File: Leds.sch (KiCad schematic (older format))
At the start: 46 parts, among them U4 MAX7219

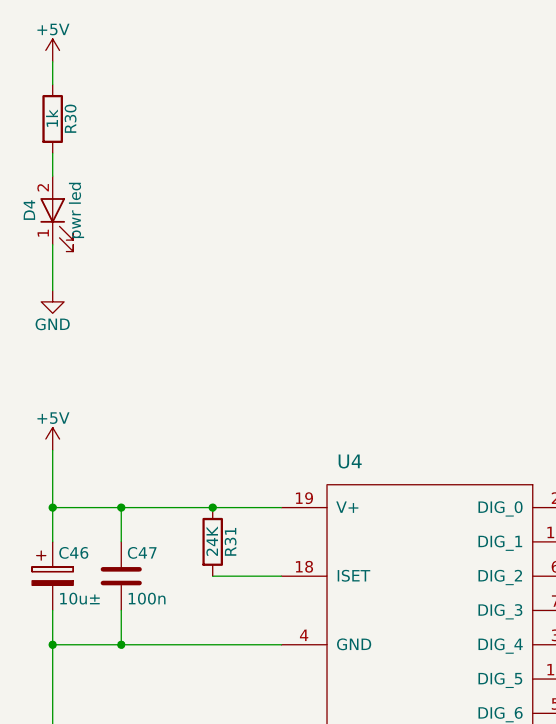
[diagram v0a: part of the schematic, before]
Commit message: Board should be ok. Bargraph leds yet to do.
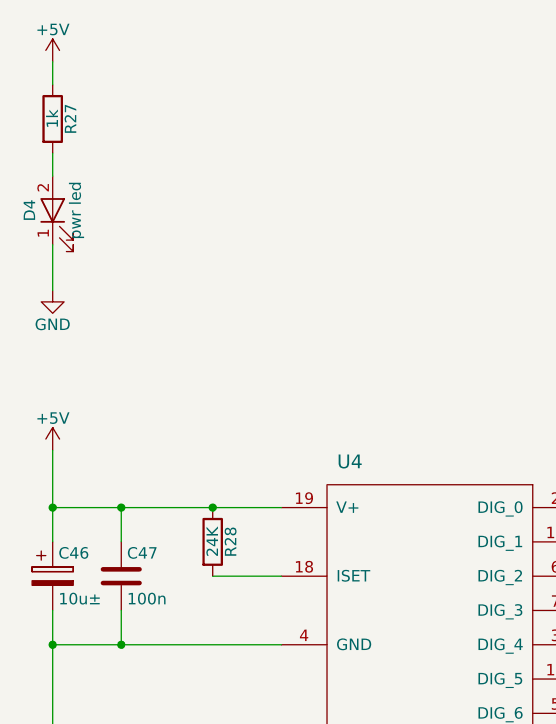
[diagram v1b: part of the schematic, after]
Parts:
- renumbered R30 to R27, R31 to R28
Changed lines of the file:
@@
 $EndComp
 $Comp
-L R R31
+L R R28
 U 1 1 59A6F7DE
 P 2450 3100
-F 0 "R31" V 2530 3100 50  0000 C CNN
+F 0 "R28" V 2530 3100 50  0000 C CNN
 F 1 "24K" V 2450 3100 50  0000 C CNN
 F 2 "Resistors_SMD:R_0603" V 2380 3100 50  0001 C CNN
@@
 	1750 2000 1750 1800
 $Comp
-L R R30
+L R R27
 U 1 1 59C8EB45
 P 1750 1250
-F 0 "R30" V 1830 1250 50  0000 C CNN
+F 0 "R27" V 1830 1250 50  0000 C CNN
 F 1 "1k" V 1750 1250 50  0000 C CNN
 F 2 "Resistors_SMD:R_0603" V 1680 1250 50  0001 C CNN

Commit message: Seems to be good for fabrication launch. Probably minor things to fix.
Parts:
- removed D43: ST_01, LEDs:LED_0603, symbol LED
- removed D44: ST_00, LEDs:LED_0603, symbol LED
- added J7: Display - secondary, Connectors_perso:Hirose_FH12-16S-1_SH, symbol Conn_01x16
- added J8: Display - main, Connectors_perso:Hirose_FH12-16S-1_SH, symbol Conn_01x16
- D10: value VU_10 -> VU_05
- D11: value VU_09 -> VU_06
- D12: value VU_08 -> VU_07
- D13: value VU_07 -> VU_08
- D14: value VU_06 -> VU_09
- D15: value VU_05 -> VU_10
- D16: value VU_04 -> VU_11
- D17: value VU_03 -> VU_12
- D18: value VU_02 -> VU_13
- D19: value VU_01 -> VU_14
- D20: value VU_00 -> VU_15
- D21: value VU_31 -> VU_16
- D22: value VU_30 -> VU_17
- D23: value VU_29 -> VU_18
- D24: value VU_28 -> VU_19
- D25: value VU_27 -> VU_20
- D26: value VU_26 -> VU_21
- D27: value VU_25 -> VU_22
- D28: value VU_24 -> VU_23
- D29: value VU_23 -> VU_24
- D30: value VU_22 -> VU_25
- D31: value VU_21 -> VU_26
- D32: value VU_20 -> VU_27
- D33: value VU_19 -> VU_28
- D34: value VU_18 -> VU_29
- D35: value VU_17 -> VU_30
- D36: value VU_16 -> VU_31
- D37: value ST_07 -> ST_00
- D38: value ST_06 -> ST_01
- D39: value ST_05 -> ST_02
- D40: value ST_04 -> ST_03
- D41: value ST_03 -> ST_04
- D42: value ST_02 -> ST_05
- D5: value VU_15 -> VU_00
- D6: value VU_14 -> VU_01
- D7: value VU_13 -> VU_02
- D8: value VU_12 -> VU_03
- D9: value VU_11 -> VU_04
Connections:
- net +5V: now also J7.15 (Pin_15), J8.2 (Pin_2)
- net DIG_0: now also D10.1 (K), D11.1 (K), D12.1 (K), D5.1 (K), D6.1 (K), D7.1 (K), D8.1 (K), D9.1 (K), J7.9 (Pin_9), J8.8 (Pin_8); no longer D13.1 (K), D14.1 (K), D15.1 (K), D16.1 (K), D17.1 (K), D18.1 (K), D19.1 (K), D20.1 (K)
- net DIG_1: now also D13.1 (K), D14.1 (K), D15.1 (K), D16.1 (K), D17.1 (K), D18.1 (K), D19.1 (K), D20.1 (K), J7.10 (Pin_10), J8.7 (Pin_7); no longer D10.1 (K), D11.1 (K), D12.1 (K), D5.1 (K), D6.1 (K), D7.1 (K), D8.1 (K), D9.1 (K)
- net DIG_2: now also D21.1 (K), D22.1 (K), D23.1 (K), D24.1 (K), D25.1 (K), D26.1 (K), D27.1 (K), D28.1 (K), J7.11 (Pin_11), J8.6 (Pin_6); no longer D29.1 (K), D30.1 (K), D31.1 (K), D32.1 (K), D33.1 (K), D34.1 (K), D35.1 (K), D36.1 (K)
- net DIG_3: now also D29.1 (K), D30.1 (K), D31.1 (K), D32.1 (K), D33.1 (K), D34.1 (K), D35.1 (K), D36.1 (K), J7.12 (Pin_12), J8.5 (Pin_5); no longer D21.1 (K), D22.1 (K), D23.1 (K), D24.1 (K), D25.1 (K), D26.1 (K), D27.1 (K), D28.1 (K)
- net DIG_4: now also J7.13 (Pin_13), J8.4 (Pin_4)
- net GND: now also J7.16 (Pin_16), J8.1 (Pin_1)
- net SEG_A: now also D11.2 (A), D19.2 (A), D27.2 (A), D35.2 (A), J7.7 (Pin_7), J8.10 (Pin_10); no longer D14.2 (A), D22.2 (A), D30.2 (A), D38.2 (A), D6.2 (A)
- net SEG_B: now also D10.2 (A), D18.2 (A), D26.2 (A), D34.2 (A), D42.2 (A), J7.6 (Pin_6), J8.11 (Pin_11); no longer D15.2 (A), D23.2 (A), D31.2 (A), D39.2 (A), D7.2 (A)
- net SEG_C: now also D17.2 (A), D25.2 (A), D33.2 (A), D41.2 (A), D9.2 (A), J7.5 (Pin_5), J8.12 (Pin_12); no longer D16.2 (A), D24.2 (A), D32.2 (A), D40.2 (A), D8.2 (A)
- net SEG_D: now also D16.2 (A), D24.2 (A), D32.2 (A), D40.2 (A), D8.2 (A), J7.4 (Pin_4), J8.13 (Pin_13); no longer D17.2 (A), D25.2 (A), D33.2 (A), D41.2 (A), D9.2 (A)
- net SEG_DP: now also D12.2 (A), D20.2 (A), D28.2 (A), D36.2 (A), J7.8 (Pin_8), J8.9 (Pin_9); no longer D13.2 (A), D21.2 (A), D29.2 (A), D37.2 (A), D5.2 (A)
- net SEG_E: now also D15.2 (A), D23.2 (A), D31.2 (A), D39.2 (A), D7.2 (A), J7.3 (Pin_3), J8.14 (Pin_14); no longer D10.2 (A), D18.2 (A), D26.2 (A), D34.2 (A), D42.2 (A)
- net SEG_F: now also D14.2 (A), D22.2 (A), D30.2 (A), D38.2 (A), D6.2 (A), J7.2 (Pin_2), J8.15 (Pin_15); no longer D11.2 (A), D19.2 (A), D27.2 (A), D35.2 (A)
- net SEG_G: now also D13.2 (A), D21.2 (A), D29.2 (A), D37.2 (A), D5.2 (A), J7.1 (Pin_1), J8.16 (Pin_16); no longer D12.2 (A), D20.2 (A), D28.2 (A), D36.2 (A)
- no-connect marks 4 -> 6
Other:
- moved on the sheet: C46, C47, D4, R27, R28, U4

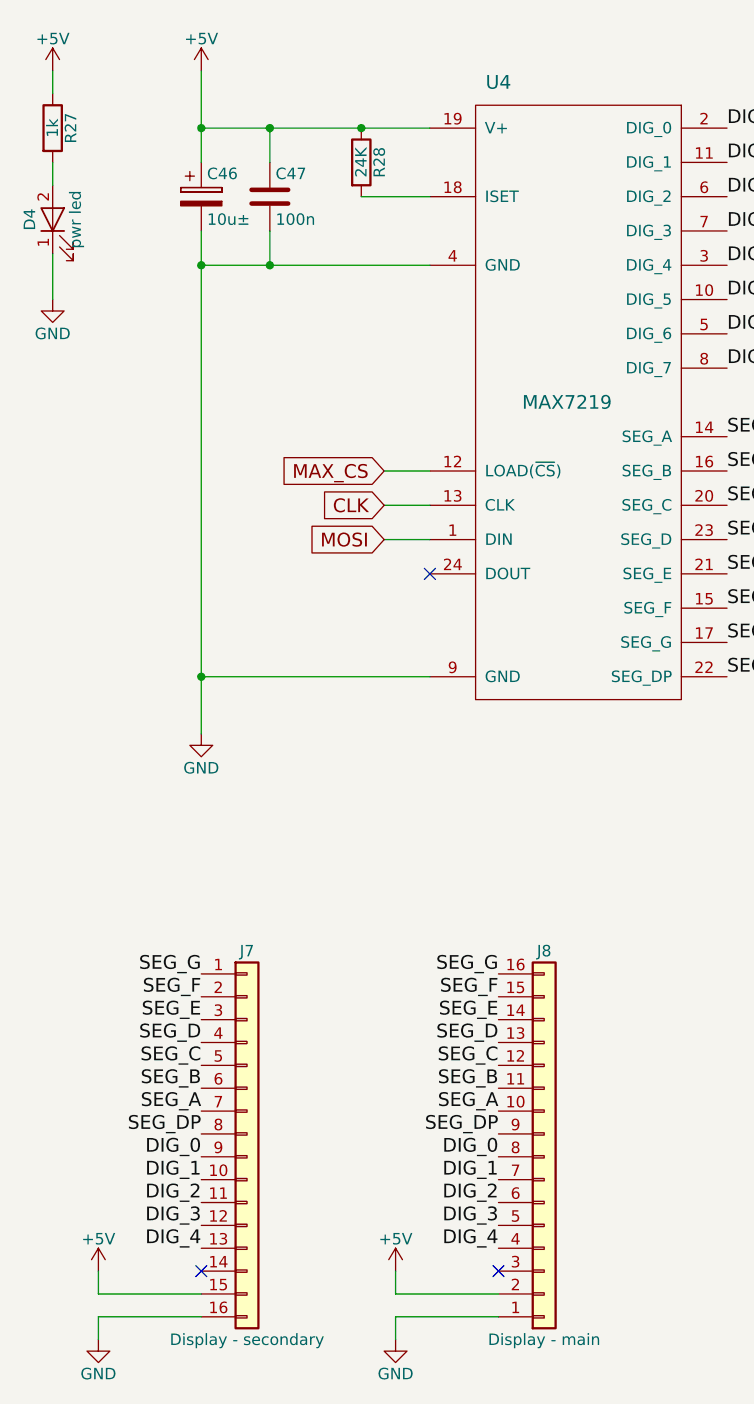
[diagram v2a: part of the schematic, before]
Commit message: Board modified after ckecking. Ready for fab, just need to create gerber, position and components files.
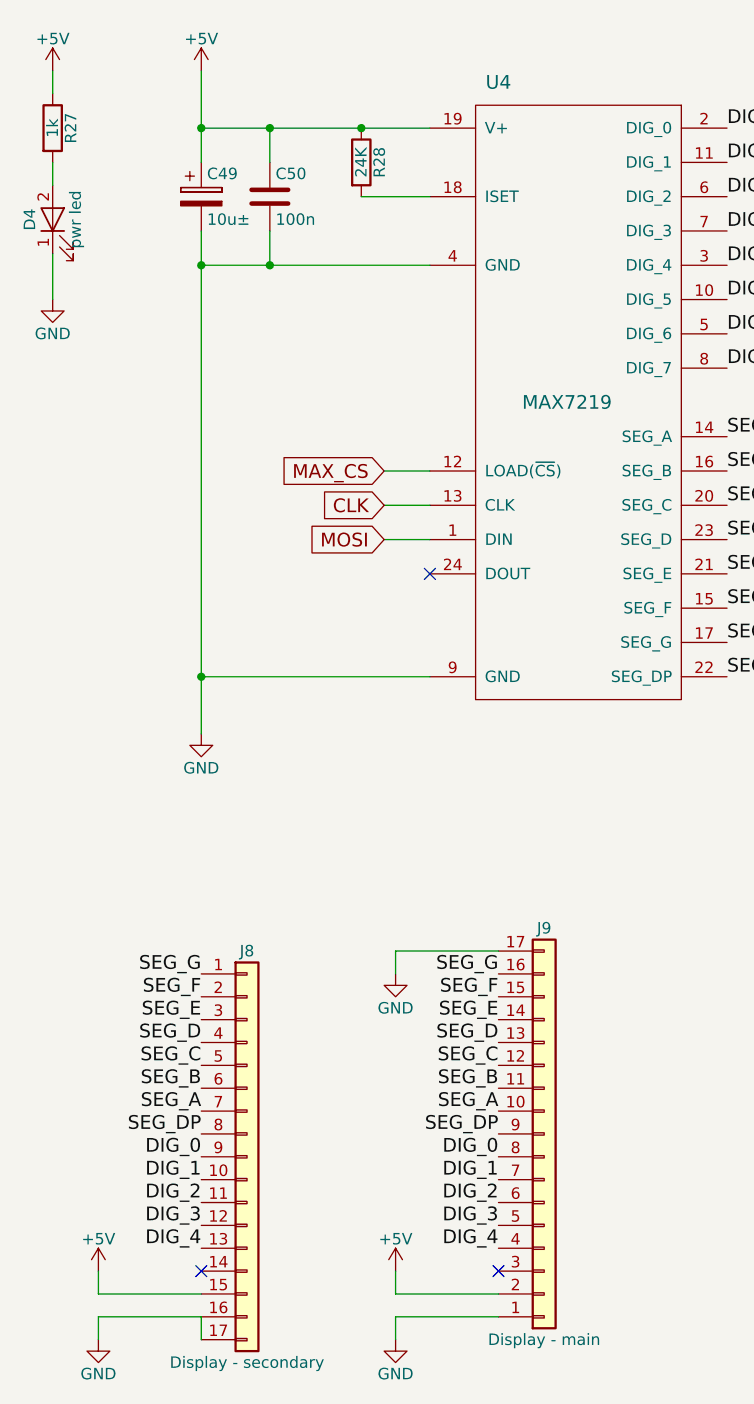
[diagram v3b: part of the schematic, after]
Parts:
- removed J7: Display - secondary, Connectors_perso:Hirose_FH12-16S-1_SH, symbol Conn_01x16
- removed J8: Display - main, Connectors_perso:Hirose_FH12-16S-1_SH, symbol Conn_01x16
- added J8: Display - secondary, Connectors_perso:Hirose_FH12-16S-1_SH, symbol Conn_01x17
- added J9: Display - main, Connectors_perso:Hirose_FH12-16S-1_SH, symbol Conn_01x17
- renumbered C46 to C49, C47 to C50
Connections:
- net +5V: now also J8.15 (Pin_15), J9.2 (Pin_2)
- net DIG_0: now also J8.9 (Pin_9), J9.8 (Pin_8)
- net DIG_1: now also J8.10 (Pin_10), J9.7 (Pin_7)
- net DIG_2: now also J8.11 (Pin_11), J9.6 (Pin_6)
- net DIG_3: now also J8.12 (Pin_12), J9.5 (Pin_5)
- net DIG_4: now also J8.13 (Pin_13), J9.4 (Pin_4)
- net GND: now also J8.16 (Pin_16), J8.17 (Pin_17), J9.1 (Pin_1), J9.17 (Pin_17)
- net SEG_A: now also J8.7 (Pin_7), J9.10 (Pin_10)
- net SEG_B: now also J8.6 (Pin_6), J9.11 (Pin_11)
- net SEG_C: now also J8.5 (Pin_5), J9.12 (Pin_12)
- net SEG_D: now also J8.4 (Pin_4), J9.13 (Pin_13)
- net SEG_DP: now also J8.8 (Pin_8), J9.9 (Pin_9)
- net SEG_E: now also J8.3 (Pin_3), J9.14 (Pin_14)
- net SEG_F: now also J8.2 (Pin_2), J9.15 (Pin_15)
- net SEG_G: now also J8.1 (Pin_1), J9.16 (Pin_16)
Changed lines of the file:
@@
 EESchema Schematic File Version 2
+LIBS:ContactConsequencesMono-rescue
 LIBS:switches-perso
 LIBS:Logos
@@
 $EndComp
 $Comp
-L +5V #PWR055
+L +5V #PWR062
 U 1 1 59A6F6F7
 P 1750 1450
-F 0 "#PWR055" H 1750 1300 50  0001 C CNN
+F 0 "#PWR062" H 1750 1300 50  0001 C CNN
 F 1 "+5V" H 1750 1590 50  0000 C CNN
 F 2 "" H 1750 1450 50  0001 C CNN
@@
 $EndComp
 $Comp
-L GND #PWR056
+L GND #PWR063
 U 1 1 59A6F70D
 P 1750 4350
-F 0 "#PWR056" H 1750 4100 50  0001 C CNN
+F 0 "#PWR063" H 1750 4100 50  0001 C CNN
 F 1 "GND" H 1750 4200 50  0000 C CNN
 F 2 "" H 1750 4350 50  0001 C CNN
@@
 Connection ~ 1750 4100
 $Comp
-L C C47
+L C C50
 U 1 1 59A6F75A
 P 2050 2000
-F 0 "C47" H 2075 2100 50  0000 L CNN
+F 0 "C50" H 2075 2100 50  0000 L CNN
 F 1 "100n" H 2075 1900 50  0000 L CNN
 F 2 "Capacitors_SMD:C_0603" H 2088 1850 50  0001 C CNN
@@
 	2550 3500 2750 3500
 $Comp
-L CP C46
+L CP C49
 U 1 1 59A6FFCC
 P 1750 2000
-F 0 "C46" H 1775 2100 50  0000 L CNN
+F 0 "C49" H 1775 2100 50  0000 L CNN
 F 1 "10u±" H 1775 1900 50  0000 L CNN
 F 2 "Capacitors_Tantalum_SMD:CP_Tantalum_Case-A_EIA-3216-18_Reflow" H 1788 1850 50  0001 C CNN
@@
 $EndComp
 $Comp
-L GND #PWR057
+L GND #PWR064
 U 1 1 59C8EA42
 P 1100 2450
-F 0 "#PWR057" H 1100 2200 50  0001 C CNN
+F 0 "#PWR064" H 1100 2200 50  0001 C CNN
 F 1 "GND" H 1100 2300 50  0000 C CNN
 F 2 "" H 1100 2450 50  0001 C CNN
@@
 $EndComp
 $Comp
-L +5V #PWR058
+L +5V #PWR065
 U 1 1 59C8EBCE
 P 1100 1450
-F 0 "#PWR058" H 1100 1300 50  0001 C CNN
+F 0 "#PWR065" H 1100 1300 50  0001 C CNN
 F 1 "+5V" H 1100 1590 50  0000 C CNN
 F 2 "" H 1100 1450 50  0001 C CNN
@@
 Wire Wire Line
 	8700 1300 8700 2800
-$Comp
-L Conn_01x16 J7
-U 1 1 59CD96B4
-P 1950 6100
-F 0 "J7" H 1950 6900 50  0000 C CNN
-F 1 "Display - secondary" H 1950 5200 50  0000 C CNN
-F 2 "Connectors_perso:Hirose_FH12-16S-1_SH" H 1950 6100 50  0001 C CNN
-F 3 "" H 1950 6100 50  0001 C CNN
-	1    1950 6100
-	1    0    0    -1
-$EndComp
 Text Label 1750 6000 2    60   ~ 0
 SEG_A
@@
 DIG_0
 $Comp
-L +5V #PWR059
+L +5V #PWR066
 U 1 1 59CDB010
 P 1300 6700
-F 0 "#PWR059" H 1300 6550 50  0001 C CNN
+F 0 "#PWR066" H 1300 6550 50  0001 C CNN
 F 1 "+5V" H 1300 6840 50  0000 C CNN
 F 2 "" H 1300 6700 50  0001 C CNN
@@
 $EndComp
 $Comp
-L GND #PWR060
+L GND #PWR067
 U 1 1 59CDB07E
 P 1300 7000
-F 0 "#PWR060" H 1300 6750 50  0001 C CNN
+F 0 "#PWR067" H 1300 6750 50  0001 C CNN
 F 1 "GND" H 1300 6850 50  0000 C CNN
 F 2 "" H 1300 7000 50  0001 C CNN
@@
 	1300 6800 1300 6700
 NoConn ~ 1750 6700
-$Comp
-L Conn_01x16 J8
-U 1 1 59CDB6F9
-P 3250 6200
-F 0 "J8" H 3250 5300 50  0000 C CNN
-F 1 "Display - main" H 3250 7000 50  0000 C CNN
-F 2 "Connectors_perso:Hirose_FH12-16S-1_SH" H 3250 6200 50  0001 C CNN
-F 3 "" H 3250 6200 50  0001 C CNN
-	1    3250 6200
-	1    0    0    1
-$EndComp
 Text Label 3050 6000 2    60   ~ 0
 SEG_A
@@
 DIG_0
 $Comp
-L +5V #PWR061
+L +5V #PWR068
 U 1 1 59CDB70C
 P 2600 6700
-F 0 "#PWR061" H 2600 6550 50  0001 C CNN
+F 0 "#PWR068" H 2600 6550 50  0001 C CNN
 F 1 "+5V" H 2600 6840 50  0000 C CNN
 F 2 "" H 2600 6700 50  0001 C CNN
@@
 $EndComp
 $Comp
-L GND #PWR062
+L GND #PWR069
 U 1 1 59CDB712
 P 2600 7000
-F 0 "#PWR062" H 2600 6750 50  0001 C CNN
+F 0 "#PWR069" H 2600 6750 50  0001 C CNN
 F 1 "GND" H 2600 6850 50  0000 C CNN
 F 2 "" H 2600 7000 50  0001 C CNN
@@
 	2600 6800 2600 6700
 NoConn ~ 3050 6700
+$Comp
+L Conn_01x17 J8
+U 1 1 59CE1A5B
+P 1950 6200
+F 0 "J8" H 1950 7100 50  0000 C CNN
+F 1 "Display - secondary" H 1950 5300 50  0000 C CNN
+F 2 "Connectors_perso:Hirose_FH12-16S-1_SH" H 1950 6200 50  0001 C CNN
+F 3 "" H 1950 6200 50  0001 C CNN
+	1    1950 6200
+	1    0    0    -1
+$EndComp
+Wire Wire Line
+	1750 6900 1750 7000
+$Comp
+L Conn_01x17 J9
+U 1 1 59CE1D20
+P 3250 6100
+F 0 "J9" H 3250 5200 50  0000 C CNN
+F 1 "Display - main" H 3250 7000 50  0000 C CNN
+F 2 "Connectors_perso:Hirose_FH12-16S-1_SH" H 3250 6100 50  0001 C CNN
+F 3 "" H 3250 6100 50  0001 C CNN
+	1    3250 6100
+	1    0    0    1
+$EndComp
+$Comp
+L GND #PWR070
+U 1 1 59CE1DFC
+P 2600 5400
+F 0 "#PWR070" H 2600 5150 50  0001 C CNN
+F 1 "GND" H 2600 5250 50  0000 C CNN
+F 2 "" H 2600 5400 50  0001 C CNN
+F 3 "" H 2600 5400 50  0001 C CNN
+	1    2600 5400
+	1    0    0    -1
+$EndComp
+Wire Wire Line
+	2600 5400 2600 5300
+Wire Wire Line
+	2600 5300 3050 5300
 $EndSCHEMATC

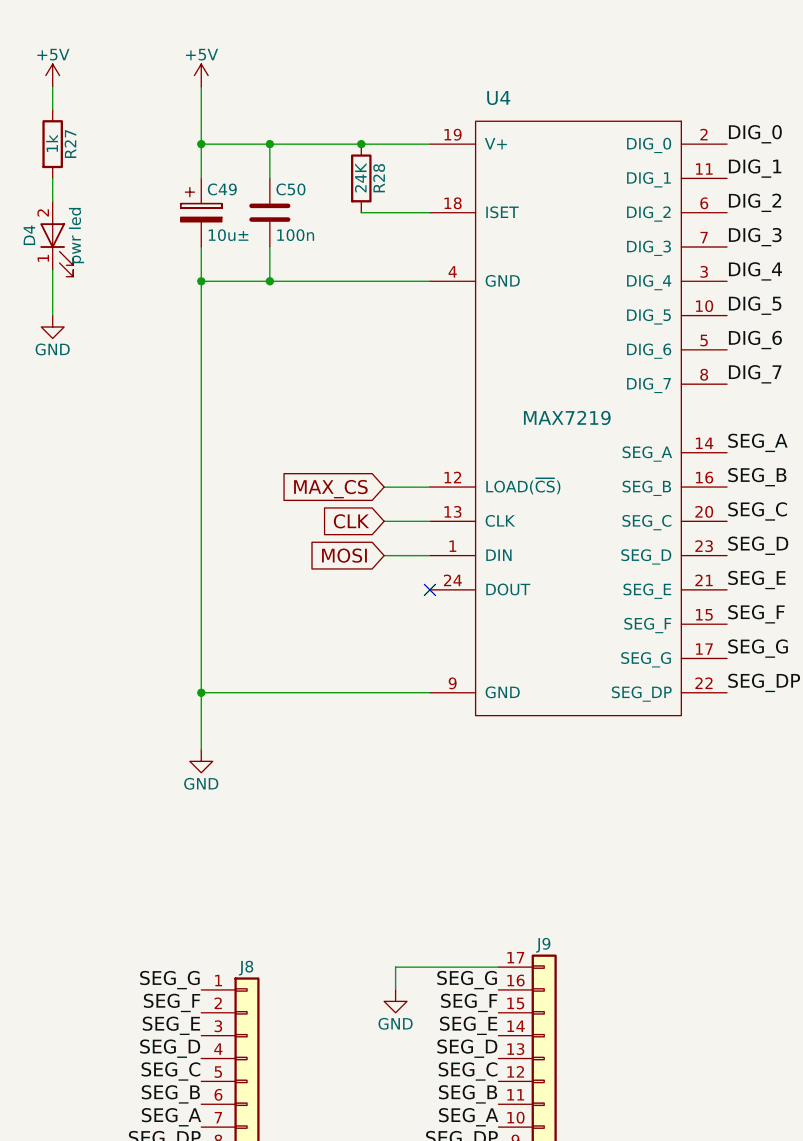
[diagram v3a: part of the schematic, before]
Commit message: v0.2 ready for fabrication. Voltage regulators replaced by cheaper ones.
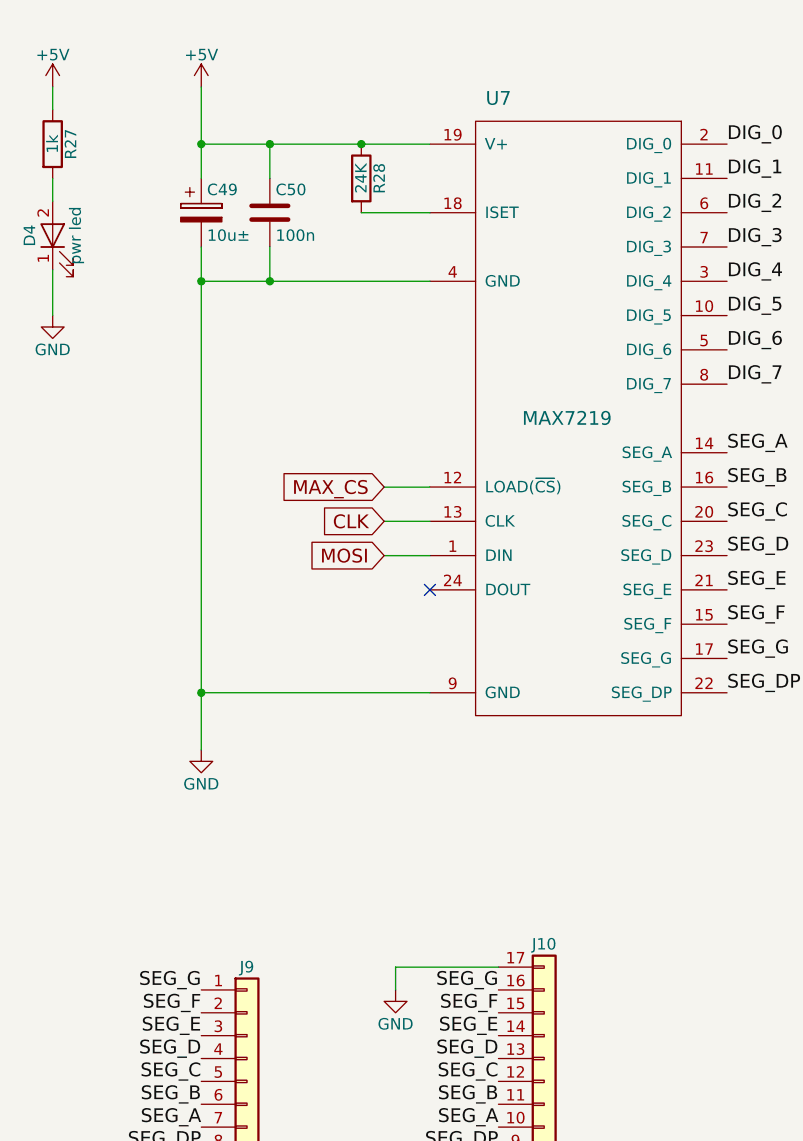
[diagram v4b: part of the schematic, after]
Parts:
- renumbered J9 to J10, J8 to J9, U4 to U7
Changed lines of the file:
@@
 $EndDescr
 $Comp
-L MAX7219 U4
+L MAX7219 U7
 U 1 1 59A6F4E2
 P 3350 2900
-F 0 "U4" H 3050 4300 60  0000 C CNN
+F 0 "U7" H 3050 4300 60  0000 C CNN
 F 1 "MAX7219" H 3350 2900 60  0000 C CNN
 F 2 "Housings_SOIC:SOIC-24W_7.5x15.4mm_Pitch1.27mm" H 3350 2900 60  0001 C CNN
@@
 NoConn ~ 3050 6700
 $Comp
-L Conn_01x17 J8
+L Conn_01x17 J9
 U 1 1 59CE1A5B
 P 1950 6200
-F 0 "J8" H 1950 7100 50  0000 C CNN
+F 0 "J9" H 1950 7100 50  0000 C CNN
 F 1 "Display - secondary" H 1950 5300 50  0000 C CNN
 F 2 "Connectors_perso:Hirose_FH12-16S-1_SH" H 1950 6200 50  0001 C CNN
@@
 	1750 6900 1750 7000
 $Comp
-L Conn_01x17 J9
+L Conn_01x17 J10
 U 1 1 59CE1D20
 P 3250 6100
-F 0 "J9" H 3250 5200 50  0000 C CNN
+F 0 "J10" H 3250 5200 50  0000 C CNN
 F 1 "Display - main" H 3250 7000 50  0000 C CNN
 F 2 "Connectors_perso:Hirose_FH12-16S-1_SH" H 3250 6100 50  0001 C CNN
